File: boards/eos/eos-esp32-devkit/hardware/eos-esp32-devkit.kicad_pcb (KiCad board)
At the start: 2 copper layers, 27.9 x 48.8 mm, 36 parts, among them J1 USB-C, J2 J2, J3 J3, Q1 MMBT3904, Q2 MMBT3904, SW1 EN, SW2 BOOT, U1 ESP32-WROOM-32E-N4, U2 USBLC6-2SC6, U3 AP7361C-33, U4 CP2102N-A02-GQFN24

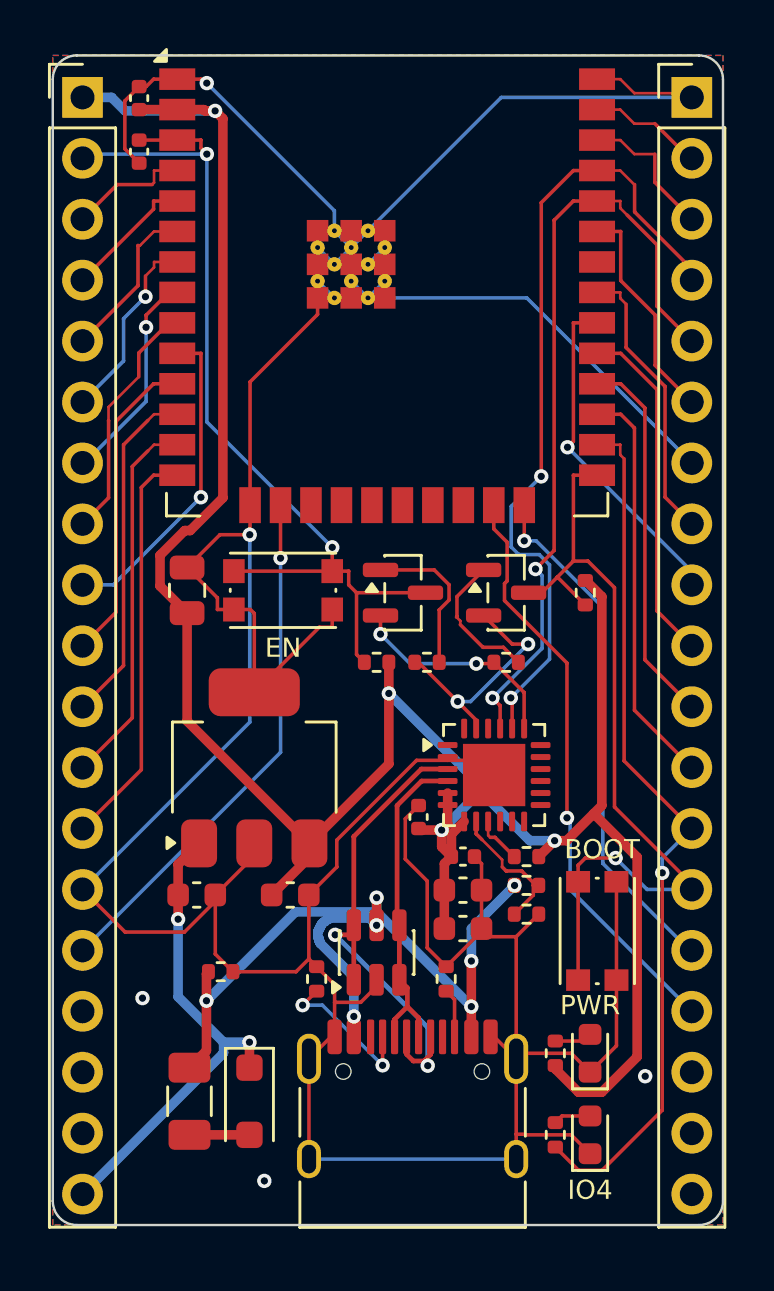
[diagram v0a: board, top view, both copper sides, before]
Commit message: fix(boards): SP0503BAHTG ESD on EoS ESP32 DevKit; footprint BOM flag follows its symbol
- EoS ESP32 DevKit: the USBLC6-2SC6 is replaced with a Littelfuse SP0503BAHTG.
  - The USBLC6's data-line diodes run to its VBUS pin. After a host unplugs, the CP2102N's
    still-live D+ pull-up (the board can run from its 5V pin) would hold VBUS near 2 V, between
    the CP2102N VBUS pin's low and high thresholds (Table 3.7), so the bridge might never see the
    unplug.
  - The SP0503BAHTG is three diodes to ground with no path between the lines. It is the part the
    CP2102N data sheet shows on its USB pins (Figure 2.5).
  - D- goes on the pad nearer the connector, so the pair reaches the CP2102N (D+ above D-)
    without crossing.
  - Rebuilt: ERC 0, DRC errors 0, unconnected 0, parity 0, 8 silkscreen-at-edge warnings.
- tools/eos_boards: each footprint's "exclude from BOM" now follows its symbol's in_bom, as
  KiCad's Update PCB from Schematic does. A library test point otherwise excludes itself while
  its symbol counts it, and parity reports the mismatch. Tested in SpecTest.
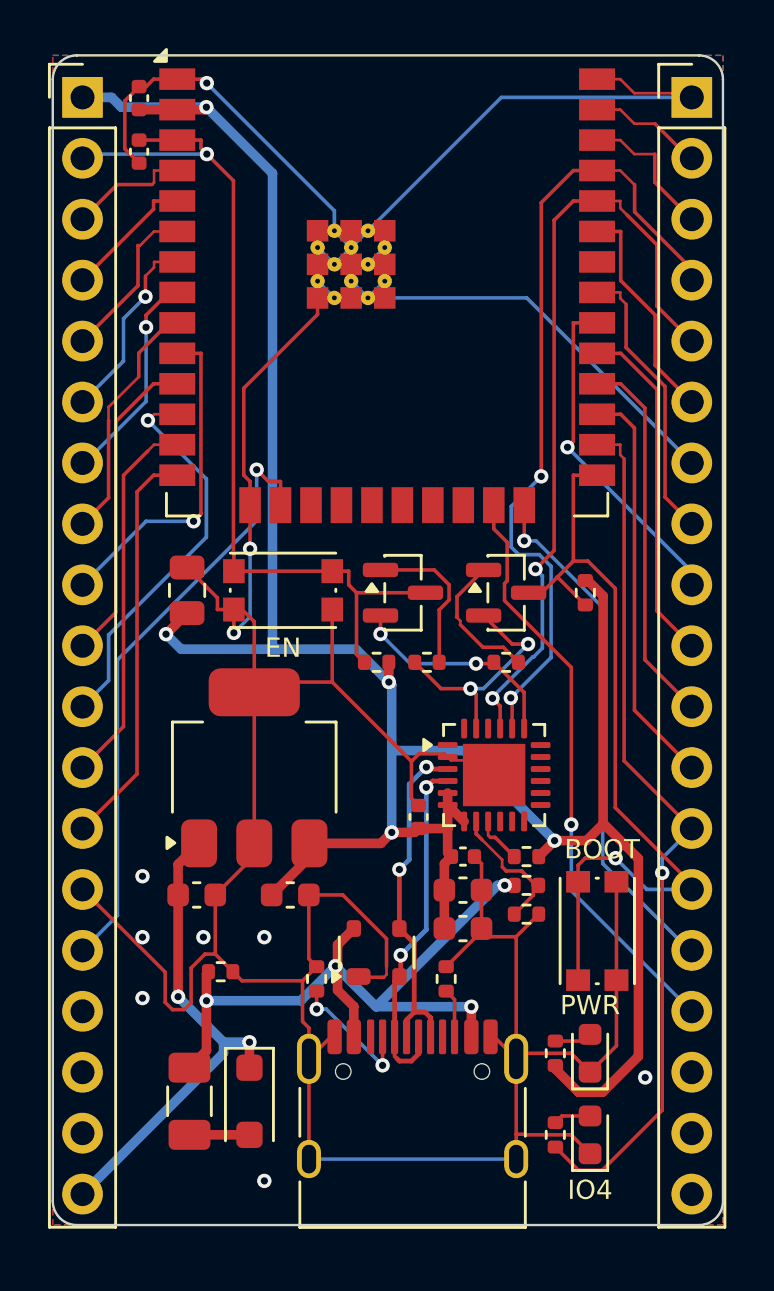
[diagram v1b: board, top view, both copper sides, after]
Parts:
- U2: value USBLC6-2SC6 -> SP0503BAHTG; footprint Package_TO_SOT_SMD:SOT-23-6 -> Package_TO_SOT_SMD:SOT-143
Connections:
- U2 pad 1: /USB_D+ -> GND
- U2 pad 2: GND -> /USB_D-
- U2 pad 3: /USB_D- -> /USB_D+
- U2 pad 4: /USB_D- -> VBUS
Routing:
- net GND: track 204.8 -> 197.1 mm, vias 5 -> 10
- net /USB_D+: track 21.8 -> 14.6 mm
- net VBUS: track 35.3 -> 30.9 mm, vias 7 -> 4
- net /IO13: track 22.0 -> 25.2 mm
- net /IO27: track 14.4 -> 16.4 mm, vias 0 -> 1
- net /EN: track 39.8 -> 38.1 mm, vias 2 -> 1
- net +3V3: track 104.4 -> 103.1 mm, vias 4 -> 5
- net /CC1: track 6.39 -> 5.66 mm
- net /USB_D-: track 14.0 -> 14.7 mm, vias 0 -> 2

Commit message: fix(boards): USB-C at HRO's edge distance on EoS CM4 Base and EoS ESP32 DevKit
Both now place their HRO TYPE-C-31-M-12 at design.USB_C_EDGE (3.19 mm from
the edge it faces), as the first four boards do since d6baf98: at 3.8 mm the
shell's face sat 0.15 mm behind the board edge, so a plug's overmold could
meet the board before the plug seated.

Rebuilt: EoS CM4 Base ERC 0, DRC errors 0, unconnected 0, parity 0, 4 DRC
warnings; EoS ESP32 DevKit the same with 8 warnings, as before.
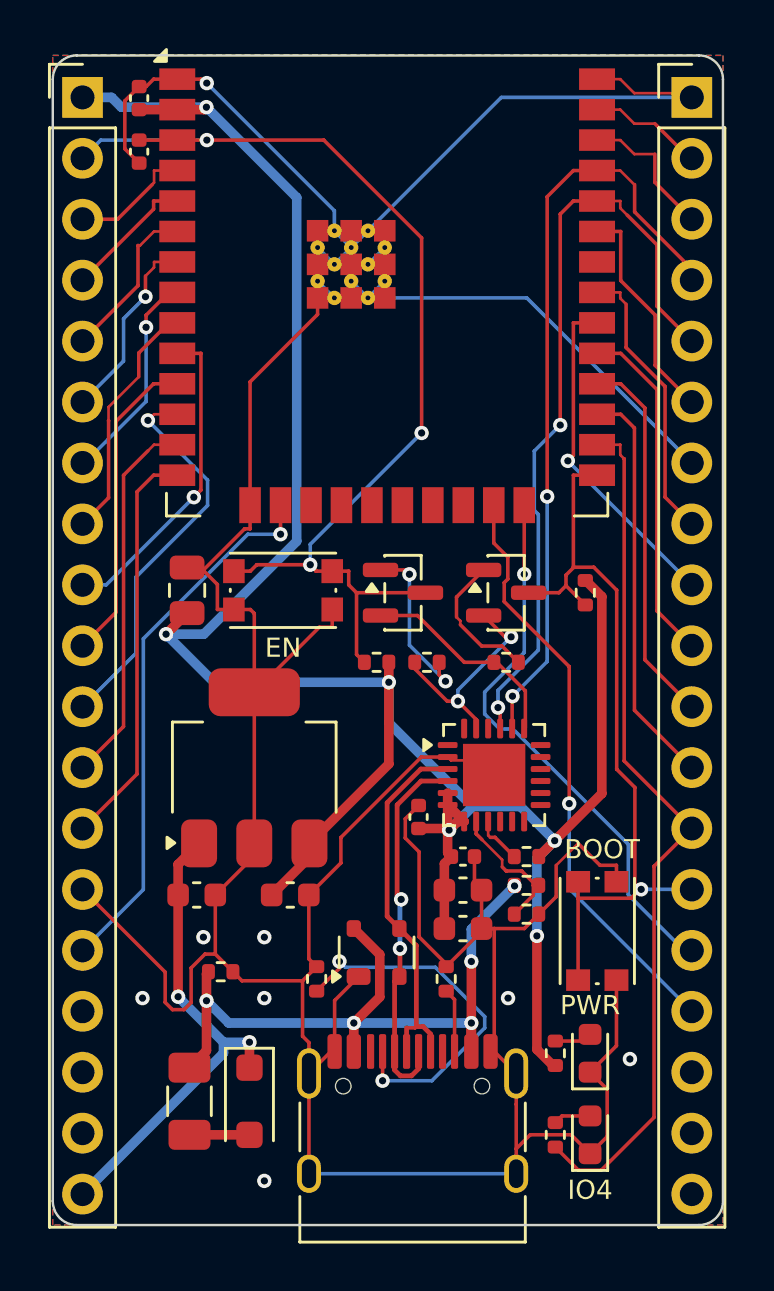
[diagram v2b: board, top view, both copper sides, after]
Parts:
- moved J1 0.61 mm to (15.0, 45.6)
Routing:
- net /CC1: track 5.66 -> 15.5 mm
- net /EN: track 38.1 -> 46.5 mm, vias 1 -> 3
- net GND: track 197.1 -> 201.4 mm, vias 10 -> 8
- net /IO13: track 25.2 -> 22.8 mm
- net /IO0: track 34.9 -> 32.6 mm
- net /U0TXD: track 34.0 -> 32.1 mm
- net /IO2: track 21.8 -> 23.3 mm
- net +3V3: track 103.1 -> 101.7 mm, vias 5 -> 6
- net /USB_D+: track 14.6 -> 15.8 mm, vias 2 -> 0
- net /USB_D-: track 14.7 -> 15.7 mm
- net /DTR: track 10.1 -> 9.20 mm
- net /QB1: track 6.52 -> 7.26 mm, vias 0 -> 2
- net /CC2: track 2.05 -> 2.66 mm
- net /IO25: track 13.8 -> 13.3 mm
- net /RTS: track 9.33 -> 8.96 mm, vias 2 -> 0
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
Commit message: fix(boards): vias in an exposed ground pad on two-layer boards too
fanout() gave a chip's exposed pad its 2 x 2 vias only on boards with an
inner plane, so on a two-layer board a QFN's centre pad reached ground
through whatever track the router left it. EoS ESP32 DevKit's CP2102N
(U4, pad 25) had no via in it. Now an exposed pad on a net poured on both
outer layers gets the same four vias, into the bottom pour; a footprint that
brings its own through-hole thermal vias (Raspberry Pi's RP2350A, Espressif's
modules) gets none added.

EoS ESP32 DevKit rebuilt: ERC 0, DRC errors 0, unconnected 0, parity 0,
8 DRC warnings as before. ExposedPadTest checks every board; it failed on
the old ESP32 DevKit (U4.25) and passes on all boards now.

Found in the independent review of a later board (EoS RA2E1 Board, M1).
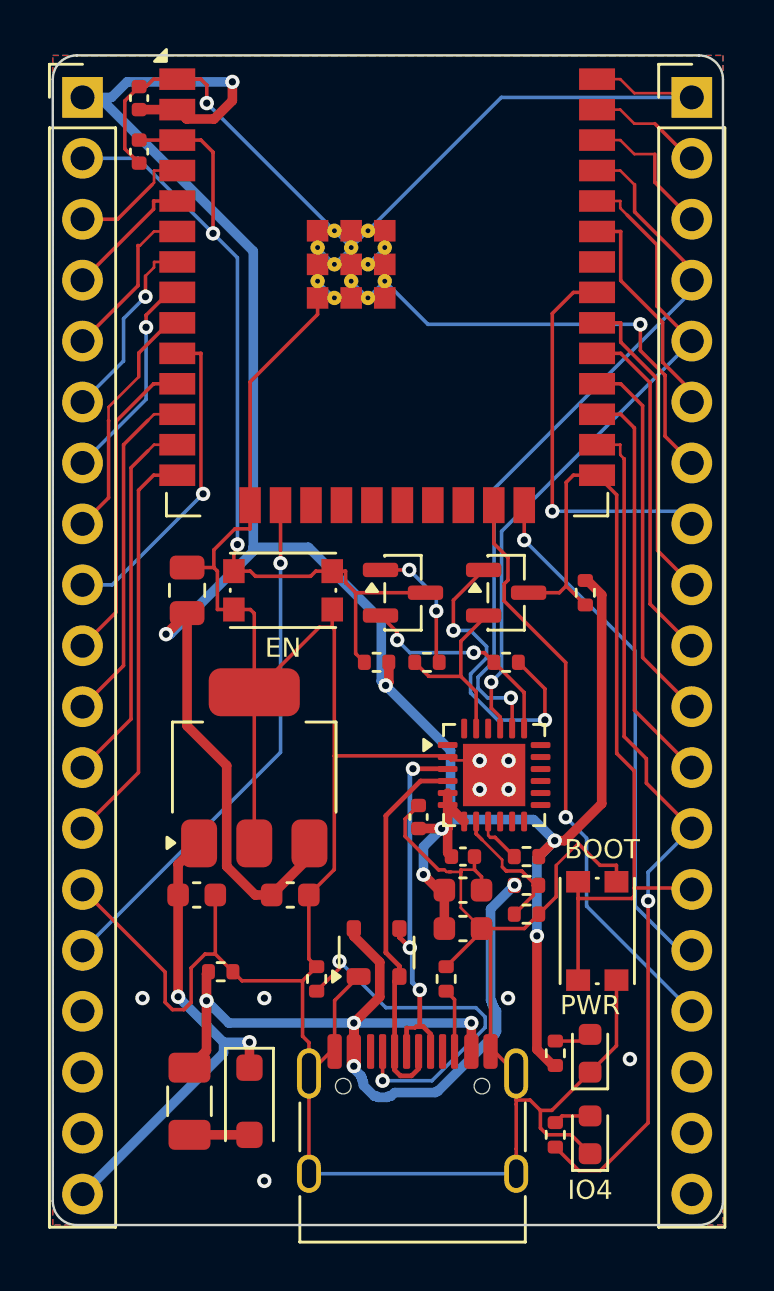
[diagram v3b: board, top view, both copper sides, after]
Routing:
- net +3V3: track 101.7 -> 111.5 mm, vias 6 -> 7
- net VBUS: track 30.6 -> 39.3 mm
- net GND: track 201.4 -> 209.5 mm, vias 8 -> 11
- net /QB2: track 5.89 -> 13.4 mm, vias 0 -> 2
- net /EN: track 46.5 -> 39.8 mm, vias 3 -> 2
- net /U0RXD: track 32.5 -> 27.8 mm, vias 2 -> 1
- net /IO19: track 11.9 -> 16.5 mm, vias 0 -> 1
- net /IO0: track 32.6 -> 35.6 mm, vias 1 -> 0
- net /IO27: track 16.5 -> 14.4 mm, vias 1 -> 0
- net /U0TXD: track 32.1 -> 30.3 mm, vias 2 -> 1
- net /QB1: track 7.26 -> 5.57 mm
- net /DTR: track 9.20 -> 7.54 mm, vias 2 -> 0
- net /IO2: track 23.3 -> 21.8 mm
- net /IO18: track 14.1 -> 13.1 mm, vias 1 -> 0
- net /IO13: track 22.8 -> 22.0 mm
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
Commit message: fix(boards): rebuild the ten boards made before the no-via-in-pad rule (#55)
PR #64's generator keeps vias out of surface pads (a chip's exposed pad
aside) and 0.1 mm from their own net's pads. Ten boards on master were built
before that rule and had 34 pads with a via in or beside them. They are
rebuilt with the same generator: ATmega328P, RA2E1, KE16Z, KL25, STM32 64,
ESP32 DevKit, Learn RP2350, LPC55S69, CM4 Base and CM5 Base. Each builds at
ERC 0, DRC errors 0, unconnected 0 and parity 0, with the same parts, values,
nets and positions and the same DRC warnings as before.

Where the router could no longer close a short link without a via in a pad,
or left a ground pad without a good path to a via, the design files use
routing options only: priority routes, fanout_first, ground_vias, and a
bottom-layer router keep-out under KL25's crystal (so RESET_b no longer runs
under it). ViaInPadTest drops BUILT_BEFORE_THE_RULE; it now allows only Learn
RP2350's two Raspberry Pi reference vias, named by position. READMEs, TASKS
and CHANGELOG follow the rebuilt copper. Independent verification: three
rounds; the owner adopted a two-layer pour-island criterion (TASKS.md).

Part of #55.
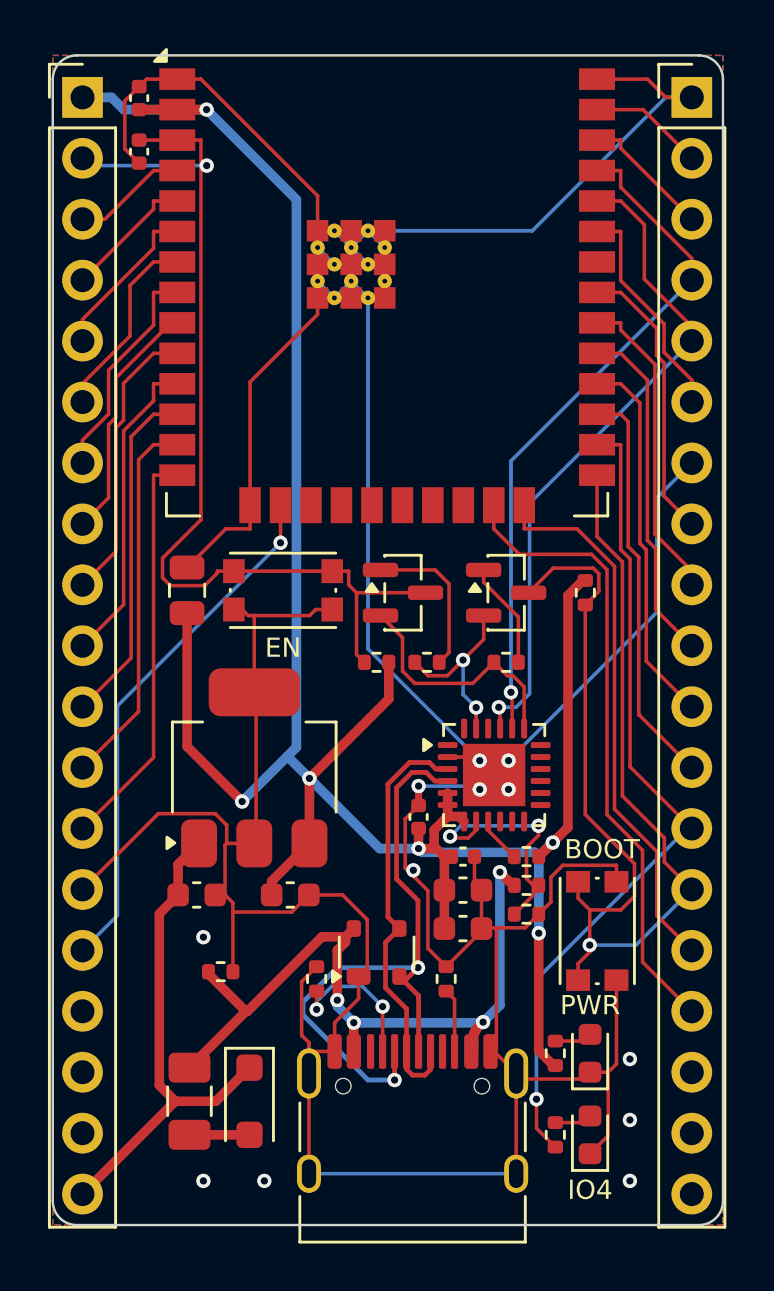
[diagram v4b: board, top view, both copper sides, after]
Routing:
- net /IO0: track 35.6 -> 48.7 mm, vias 0 -> 1
- net /USB_D-: track 16.0 -> 26.7 mm, vias 0 -> 2
- net /CC1: track 15.5 -> 6.32 mm
- net /QB2: track 13.4 -> 4.45 mm, vias 2 -> 0
- net +3V3: track 111.5 -> 103.2 mm, vias 7 -> 6
- net VBUS: track 39.3 -> 31.0 mm, vias 5 -> 4
- net GND: track 209.5 -> 214.9 mm, vias 11 -> 12
- net /IO19: track 16.5 -> 11.9 mm, vias 1 -> 0
- net /VBUS_SENSE: track 5.78 -> 10.0 mm, vias 0 -> 2
- net /EN: track 39.8 -> 42.2 mm, vias 2 -> 1
- net /IO4: track 36.3 -> 34.6 mm
- net /U0TXD: track 30.3 -> 28.6 mm
- net /IO15: track 24.6 -> 26.3 mm, vias 1 -> 0
- net /IO25: track 13.5 -> 11.9 mm, vias 1 -> 0
- net /RTS: track 9.04 -> 10.5 mm, vias 2 -> 0
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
